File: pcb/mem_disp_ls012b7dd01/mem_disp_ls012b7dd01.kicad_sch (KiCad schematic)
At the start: 4 parts, among them J1 Pin Header, J2 FCP Connector

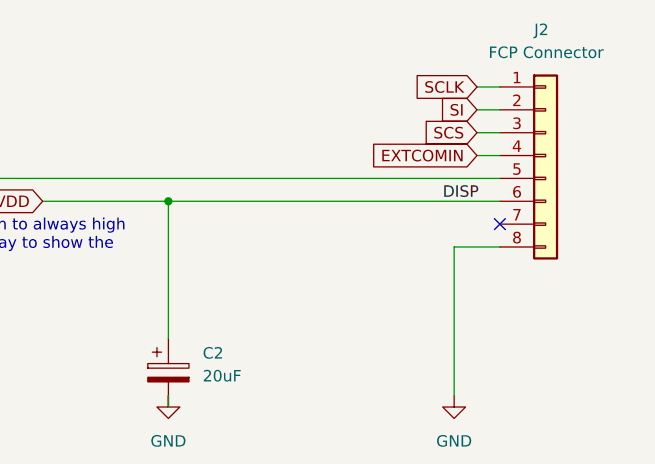
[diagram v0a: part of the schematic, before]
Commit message: Fixed capacitor mix up
VDD pin was connected to DISP capacitor and DISP capacitor was connected to VDD.

From an electrical perspective it didn’t matter though.
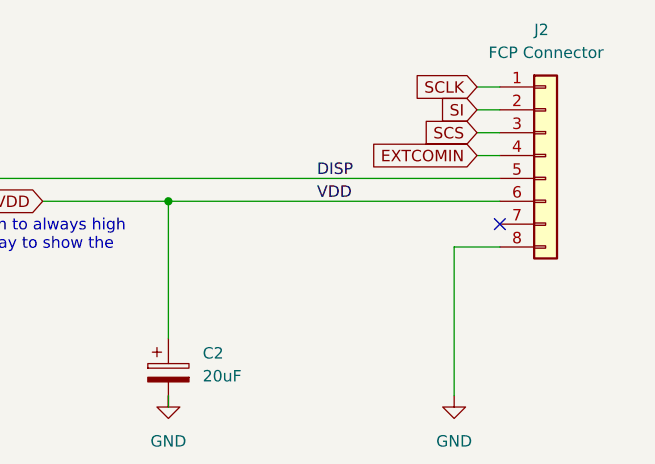
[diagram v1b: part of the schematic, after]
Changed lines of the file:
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@@
     (effects (font (size 1.27 1.27)) (justify left bottom))
   )
-  (label "DISP" (at 191.77 49.53 0)
+  (label "VDD" (at 177.8 49.53 0)
     (effects (font (size 1.27 1.27)) (justify left bottom))
   )
+  (label "DISP" (at 177.8 46.99 0)
+    (effects (font (size 1.27 1.27)) (justify left bottom))
+  )

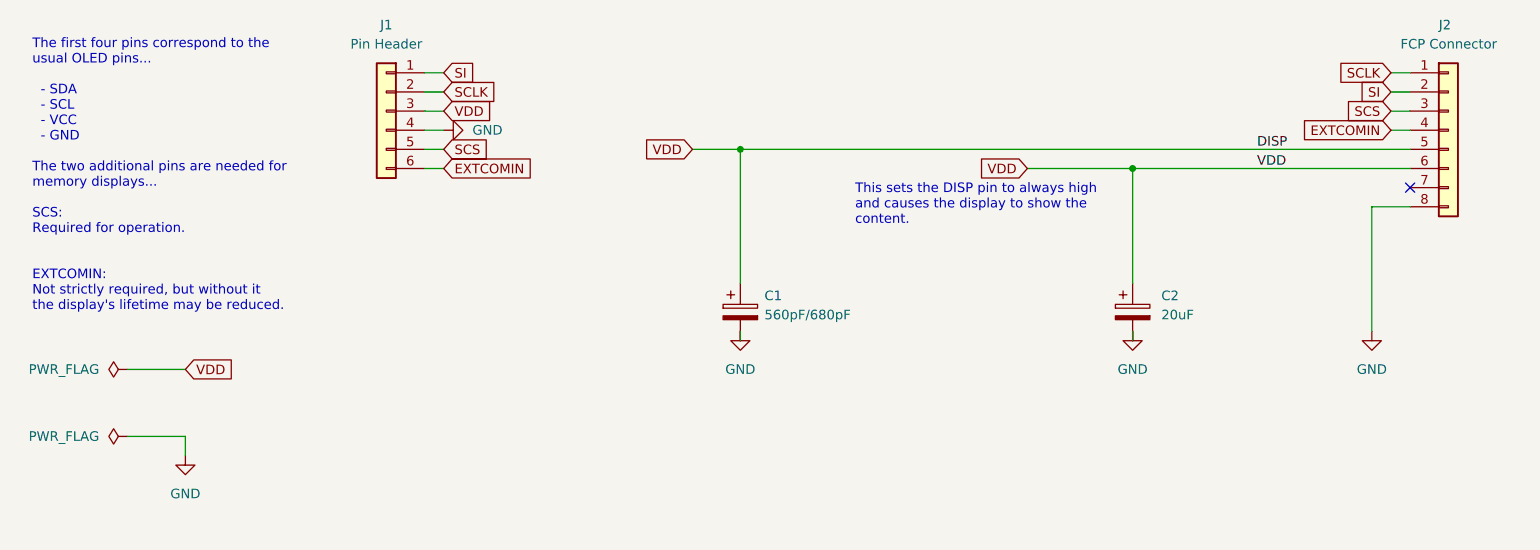
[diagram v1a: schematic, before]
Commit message: Fixed C1 capacity from 20uF to 2.0uF
The 2017 datasheet seems to show that a 20uF capacitor is requiered, but in reality 2.0uF is the correct value.

The font in the datasheet is squished, which causes the "." to merge with the
"2".

Older datasheets also show a value of 2.0.
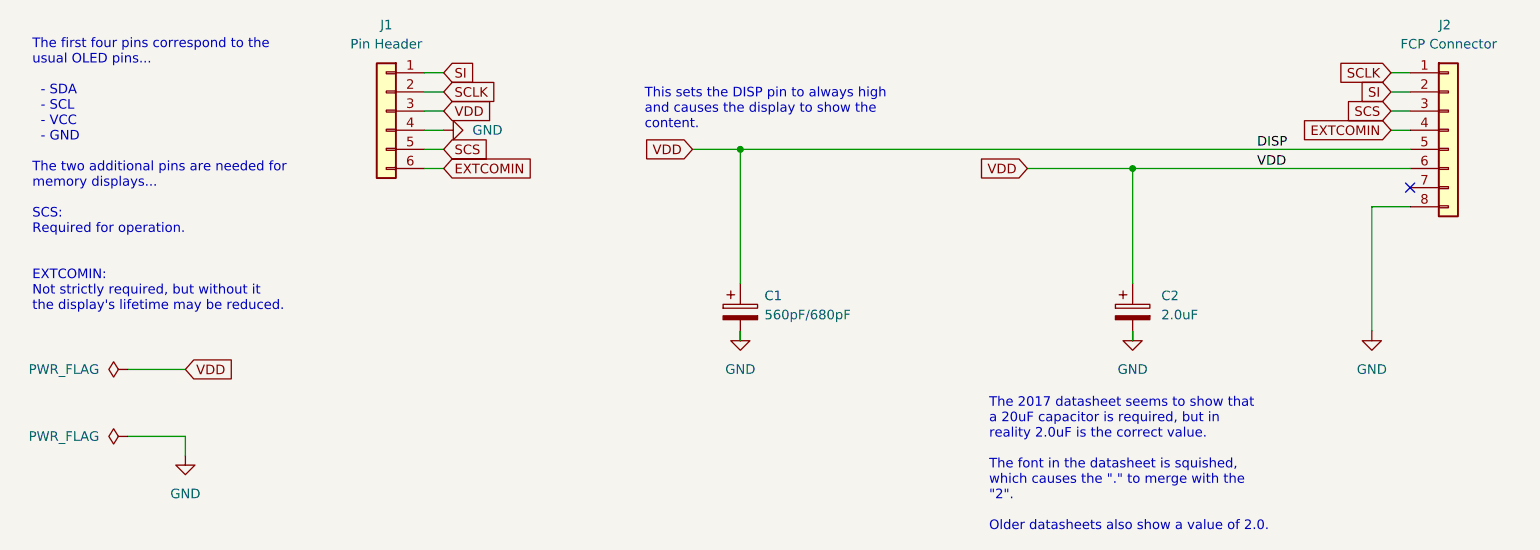
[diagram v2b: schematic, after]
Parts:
- C2: value 20uF -> 2.0uF
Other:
- note added: "The 2017 datasheet seems to show that a 20uF capacitor is required, but in reality 2.0uF is the correct value. The font in the datasheet is squished, which causes the "." to merge with the "2". Older datasheets also show a value of 2.0."
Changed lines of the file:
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@@
     (stroke (width 0) (type default) (color 0 0 0 0))
+  )
+  (text "The 2017 datasheet seems to show that\na 20uF capacitor is required, but in\nreality 2.0uF is the correct value.\n\nThe font in the datasheet is squished,\nwhich causes the \".\" to merge with the \n\"2\".\n\nOlder datasheets also show a value of 2.0."
+    (at 142.24 97.79 0)
+    (effects (font (size 1.27 1.27)) (justify left bottom))
   )
   (text "The first four pins correspond to the\nusual OLED pins...\n\n  - SDA\n  - SCL\n  - VCC\n  - GND\n\nThe two additional pins are needed for\nmemory displays...\n\nSCS:\nRequired for operation.\n\n\nEXTCOMIN:\nNot strictly required, but without it\nthe display's lifetime may be reduced."
@@
   )
   (text "This sets the DISP pin to always high\nand causes the display to show the\ncontent."
-    (at 124.46 57.15 0)
+    (at 96.52 44.45 0)
     (effects (font (size 1.27 1.27)) (justify left bottom))
   )
@@
       (effects (font (size 1.27 1.27)) (justify left))
     )
-    (property "Value" "20uF" (id 1) (at 165.1 68.9609 0)
+    (property "Value" "2.0uF" (id 1) (at 165.1 68.9609 0)
       (effects (font (size 1.27 1.27)) (justify left))
     )
@@
     )
     (path "/7ee89d17-12d2-4f80-9faa-05ab2e85805e"
-      (reference "C2") (unit 1) (value "20uF") (footprint "Capacitor_SMD:C_0603_1608Metric_Pad1.08x0.95mm_HandSolder")
+      (reference "C2") (unit 1) (value "2.0uF") (footprint "Capacitor_SMD:C_0603_1608Metric_Pad1.08x0.95mm_HandSolder")
     )
     (path "/bf3ea006-d053-4aa4-bdaa-5952aedf8d1c"

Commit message: Removed DISP C1 capacitor
The datasheet calls for a 560pF capacitor (C1) connected to DISP, but since we are connecting DISP to VDD, which already has a large capacitor, that's not necessary.
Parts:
- removed C1: 560pF/680pF, Capacitor_SMD:C_0603_1608Metric_Pad1.08x0.95mm_HandSolder, symbol Device:C_Polarized
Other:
- note added: "This sets the DISP pin to always high and causes the display to show the content. The datasheet calls for a 560pF capacitor (C1) here, but since we are connecting DISP to VDD, which already has a large capacitor, that's not necessary."
- note removed: "This sets the DISP pin to always high and causes the display to show the content."
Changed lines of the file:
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@@
   (title_block
     (title "Sharp Memory Display Breakout Board (LS012B7DD01)")
-    (date "2022-04-23")
-    (rev "v0.1")
+    (date "2022-04-26")
+    (rev "v0.2")
   )
   (junction (at 161.29 49.53) (diameter 0) (color 0 0 0 0)
-  )
-  (junction (at 109.22 46.99) (diameter 0) (color 0 0 0 0)
   )
   (no_connect (at 198.12 52.07))
@@
     (stroke (width 0) (type default) (color 0 0 0 0))
   )
-  (wire (pts (xy 109.22 46.99) (xy 198.12 46.99))
-    (stroke (width 0) (type default) (color 0 0 0 0))
-  )
   (wire (pts (xy 161.29 71.12) (xy 161.29 72.39))
     (stroke (width 0) (type default) (color 0 0 0 0))
@@
     (stroke (width 0) (type default) (color 0 0 0 0))
   )
-  (wire (pts (xy 109.22 46.99) (xy 109.22 64.77))
-    (stroke (width 0) (type default) (color 0 0 0 0))
-  )
   (wire (pts (xy 27.94 76.2) (xy 35.56 76.2))
     (stroke (width 0) (type default) (color 0 0 0 0))
@@
     (stroke (width 0) (type default) (color 0 0 0 0))
   )
-  (wire (pts (xy 109.22 71.12) (xy 109.22 72.39))
-    (stroke (width 0) (type default) (color 0 0 0 0))
-  )
   (wire (pts (xy 67.31 49.53) (xy 69.85 49.53))
     (stroke (width 0) (type default) (color 0 0 0 0))
@@
     (stroke (width 0) (type default) (color 0 0 0 0))
   )
-  (wire (pts (xy 102.87 46.99) (xy 109.22 46.99))
+  (wire (pts (xy 102.87 46.99) (xy 198.12 46.99))
     (stroke (width 0) (type default) (color 0 0 0 0))
   )
@@
     (effects (font (size 1.27 1.27)) (justify left bottom))
   )
-  (text "This sets the DISP pin to always high\nand causes the display to show the\ncontent."
-    (at 96.52 44.45 0)
+  (text "This sets the DISP pin to always high\nand causes the display to show the\ncontent.\n\nThe datasheet calls for a 560pF\ncapacitor (C1) here, but since we\nare connecting DISP to VDD, which\nalready has a large capacitor,\nthat's not necessary."
+    (at 96.52 68.58 0)
     (effects (font (size 1.27 1.27)) (justify left bottom))
   )
@@
     (pin "2")
   )
-  (symbol (lib_id "power:GND") (at 109.22 71.12 0) (unit 1)
-    (in_bom yes) (on_board yes) (fields_autoplaced)
-    (property "Reference" "#PWR0101" (id 0) (at 109.22 77.47 0)
-      (effects (font (size 1.27 1.27)) hide)
-    )
-    (property "Value" "GND" (id 1) (at 109.22 76.2 0))
-    (property "Footprint" "" (id 2) (at 109.22 71.12 0)
-      (effects (font (size 1.27 1.27)) hide)
-    )
-    (property "Datasheet" "" (id 3) (at 109.22 71.12 0)
-      (effects (font (size 1.27 1.27)) hide)
-    )
-    (pin "1")
-  )
-  (symbol (lib_id "Device:C_Polarized") (at 109.22 68.58 0) (unit 1)
-    (in_bom yes) (on_board yes)
-    (property "Reference" "C1" (id 0) (at 112.4237 66.4209 0)
-      (effects (font (size 1.27 1.27)) (justify left))
-    )
-    (property "Value" "560pF/680pF" (id 1) (at 112.4237 68.9609 0)
-      (effects (font (size 1.27 1.27)) (justify left))
-    )
-    (property "Footprint" "Capacitor_SMD:C_0603_1608Metric_Pad1.08x0.95mm_HandSolder" (id 2) (at 110.1852 72.39 0)
-      (effects (font (size 1.27 1.27)) hide)
-    )
-    (property "Datasheet" "~" (id 3) (at 109.22 68.58 0)
-      (effects (font (size 1.27 1.27)) hide)
-    )
-    (pin "1")
-    (pin "2")
-  )
   (symbol (lib_id "power:GND") (at 161.29 71.12 0) (unit 1)
     (in_bom yes) (on_board yes) (fields_autoplaced)
@@
       (reference "#PWR04") (unit 1) (value "GND") (footprint "")
     )
-    (path "/8de17356-1ff8-4f66-8774-045e13068dd5"
-      (reference "#PWR0101") (unit 1) (value "GND") (footprint "")
-    )
     (path "/e0149c33-6901-436a-b88c-026deb737d5d"
       (reference "#PWR0102") (unit 1) (value "GND") (footprint "")
     )
-    (path "/99e08a88-25cf-48d0-92db-3a19aa9b7290"
-      (reference "C1") (unit 1) (value "560pF/680pF") (footprint "Capacitor_SMD:C_0603_1608Metric_Pad1.08x0.95mm_HandSolder")
-    )
     (path "/7ee89d17-12d2-4f80-9faa-05ab2e85805e"
